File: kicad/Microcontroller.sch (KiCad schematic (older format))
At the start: 30 parts, among them CN4 Conn Vite 1,5x2, CN5 Ventola, CN6 Conn Vite 1,5x2, J7 Reset, J8 Arduino_Nano_Header, U4 MAX6675

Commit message: Schematic update
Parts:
- removed A1, B1, ENC1, OK1: CONN_01X01, symbol CONN_01X01
- removed D2, D3: 1N4148, symbol D
- removed J7: Reset, symbol CONN_01X02
- removed JP1: ~, symbol CONN_01X05
- removed R21, R22, R23: 15K, symbol R
- removed R24: 1K, symbol R
- removed R25: 10K, symbol R
- gave numbers to parts that had none: 2
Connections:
- net labels added: SCK
- net labels removed: CLK, DO, RB3, RB4, RB5, RB6
- wire segments 87 -> 56
- no-connect marks 21 -> 20

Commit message: Modified the Kicad schematic adding the reset to I2c controller
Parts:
- removed R24: R, symbol R
- R25: value R -> 15K
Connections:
- net labels added: Reset
- wire segments 56 -> 53
- no-connect marks 20 -> 17
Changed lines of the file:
@@
-EESchema Schematic File Version 3
+EESchema Schematic File Version 2
 LIBS:HotAirGun-rescue
 LIBS:power
 LIBS:device
+LIBS:transistors
+LIBS:conn
 LIBS:linear
 LIBS:regul
+LIBS:74xx
+LIBS:cmos4000
 LIBS:adc-dac
 LIBS:memory
@@
 LIBS:digital-audio
 LIBS:philips
+LIBS:display
 LIBS:cypress
 LIBS:siliconi
@@
 LIBS:atmel
 LIBS:contrib
-LIBS:w_connectors
+LIBS:valves
 LIBS:max6675
 LIBS:lcd16x2
+LIBS:switches
 LIBS:HotAirGun-cache
-EELAYER 26 0
+EELAYER 25 0
 EELAYER END
 $Descr A4 11693 8268
@@
 L Arduino_Nano_Header J8
 U 1 1 59BC3AFF
-P 5580 4170
-F 0 "J8" H 5580 5107 60  0000 C CNN
-F 1 "Arduino_Nano_Header" H 5580 5001 60  0000 C CNN
-F 2 "" H 5580 4170 60  0000 C CNN
-F 3 "" H 5580 4170 60  0000 C CNN
-	1    5580 4170
-	1    0    0    -1
-$EndComp
-Text GLabel 4535 4270 0    60   Input ~ 0
+P 5670 4230
+F 0 "J8" H 5670 5167 60  0000 C CNN
+F 1 "Arduino_Nano_Header" H 5670 5061 60  0000 C CNN
+F 2 "" H 5670 4230 60  0000 C CNN
+F 3 "" H 5670 4230 60  0000 C CNN
+	1    5670 4230
+	1    0    0    -1
+$EndComp
+Text GLabel 4625 4330 0    60   Input ~ 0
 CS
-Text GLabel 4580 4370 0    60   Input ~ 0
+Text GLabel 4670 4430 0    60   Input ~ 0
 SCK
-Text GLabel 4530 4170 0    60   Input ~ 0
+Text GLabel 4620 4230 0    60   Input ~ 0
 SO
-Text GLabel 6530 4170 2    60   Input ~ 0
+Text GLabel 6620 4230 2    60   Input ~ 0
 SDA
-Text GLabel 6535 4070 2    60   Input ~ 0
+Text GLabel 6625 4130 2    60   Input ~ 0
 SCL
-Text GLabel 4730 3870 0    60   Input ~ 0
+Text GLabel 4820 3930 0    60   Input ~ 0
 FASE_0
-Text GLabel 4580 4770 0    60   Input ~ 0
+Text GLabel 4670 4830 0    60   Input ~ 0
 FAN
-Text GLabel 5090 4470 0    60   Input ~ 0
+Text GLabel 5180 4530 0    60   Input ~ 0
 RELE_SIC_220V
-Text GLabel 4655 4570 0    60   Input ~ 0
+Text GLabel 4745 4630 0    60   Input ~ 0
 TRIAC
 Wire Wire Line
-	6530 4170 5930 4170
-Wire Wire Line
-	4730 3870 5230 3870
-Wire Wire Line
-	4655 4570 5230 4570
-Wire Wire Line
-	5090 4470 5230 4470
+	6620 4230 6020 4230
+Wire Wire Line
+	4820 3930 5320 3930
+Wire Wire Line
+	4745 4630 5320 4630
+Wire Wire Line
+	5180 4530 5320 4530
 $Comp
 L GND #GND_07
@@
 Wire Wire Line
 	4825 6620 4825 6570
-NoConn ~ 5230 3470
-NoConn ~ 5230 3570
-NoConn ~ 5230 3670
-NoConn ~ 5230 3770
-NoConn ~ 5230 4070
-NoConn ~ 5230 4670
-NoConn ~ 5930 4770
-NoConn ~ 5930 4670
-NoConn ~ 5930 4570
-NoConn ~ 5930 4470
-NoConn ~ 5930 4270
-NoConn ~ 5930 3970
-NoConn ~ 5930 3870
-NoConn ~ 5930 3770
-NoConn ~ 5930 3670
-NoConn ~ 5930 3570
-NoConn ~ 5930 3470
-NoConn ~ 5930 4370
-Text GLabel 4785 3970 0    60   Input ~ 0
+NoConn ~ 5320 3530
+NoConn ~ 5320 3630
+NoConn ~ 5320 3730
+NoConn ~ 5320 3830
+NoConn ~ 5320 4130
+NoConn ~ 5320 4730
+NoConn ~ 6020 4830
+NoConn ~ 6020 4730
+NoConn ~ 6020 4630
+NoConn ~ 6020 4530
+NoConn ~ 6020 4330
+NoConn ~ 6020 4030
+NoConn ~ 6020 3930
+NoConn ~ 6020 4430
+Text GLabel 4875 4030 0    60   Input ~ 0
 MCP_INT
 Wire Wire Line
-	4785 3970 5230 3970
-$Comp
-L R R24
-U 1 1 59C972CE
-P 4885 3645
-F 0 "R24" H 4816 3599 50  0000 R CNN
-F 1 "R" H 4816 3690 50  0000 R CNN
-F 2 "" V 4815 3645 50  0001 C CNN
-F 3 "" H 4885 3645 50  0001 C CNN
-	1    4885 3645
-	1    0    0    1
-$EndComp
+	4875 4030 5320 4030
 $Comp
 L R R25
 U 1 1 59C973F4
-P 5035 3645
-F 0 "R25" H 5105 3691 50  0000 L CNN
-F 1 "R" H 5105 3600 50  0000 L CNN
-F 2 "" V 4965 3645 50  0001 C CNN
-F 3 "" H 5035 3645 50  0001 C CNN
-	1    5035 3645
-	1    0    0    -1
-$EndComp
-Wire Wire Line
-	4885 3795 4885 3970
-Connection ~ 4885 3970
-Wire Wire Line
-	5035 3795 5035 3870
-Connection ~ 5035 3870
-$Comp
-L VCC #PWR?
-U 1 1 59C97A40
-P 4955 3385
-F 0 "#PWR?" H 4955 3235 50  0001 C CNN
-F 1 "VCC" H 4955 3535 50  0000 C CNN
-F 2 "" H 4955 3385 50  0000 C CNN
-F 3 "" H 4955 3385 50  0000 C CNN
-	1    4955 3385
-	1    0    0    -1
-$EndComp
-Wire Wire Line
-	4885 3420 5035 3420
-Wire Wire Line
-	4885 3420 4885 3495
-Wire Wire Line
-	5035 3420 5035 3495
-Connection ~ 4955 3420
-Wire Wire Line
-	4955 3385 4955 3425
-Wire Wire Line
-	4580 4370 5230 4370
-Wire Wire Line
-	5230 4270 4535 4270
-Wire Wire Line
-	4530 4170 5230 4170
-Wire Wire Line
-	5230 4770 4580 4770
-Wire Wire Line
-	5930 4070 6535 4070
+P 5030 3658
+F 0 "R25" H 5100 3704 50  0000 L CNN
+F 1 "15K" H 5100 3613 50  0000 L CNN
+F 2 "" V 4960 3658 50  0001 C CNN
+F 3 "" H 5030 3658 50  0001 C CNN
+	1    5030 3658
+	1    0    0    -1
+$EndComp
+Wire Wire Line
+	4670 4430 5320 4430
+Wire Wire Line
+	5320 4330 4625 4330
+Wire Wire Line
+	4620 4230 5320 4230
+Wire Wire Line
+	5320 4830 4670 4830
+Wire Wire Line
+	6020 4130 6625 4130
 $Comp
 L GND #PWR?
@@
 Wire Wire Line
 	10190 1350 10190 1425
-NoConn ~ 5930 4870
-NoConn ~ 5230 4870
+NoConn ~ 6020 4930
+NoConn ~ 5320 4930
+$Comp
+L VCC #PWR?
+U 1 1 59F9064F
+P 5030 3470
+F 0 "#PWR?" H 5030 3320 50  0001 C CNN
+F 1 "VCC" H 5030 3620 50  0000 C CNN
+F 2 "" H 5030 3470 50  0000 C CNN
+F 3 "" H 5030 3470 50  0000 C CNN
+	1    5030 3470
+	1    0    0    -1
+$EndComp
+Wire Wire Line
+	5030 3470 5030 3520
+Wire Wire Line
+	5030 3810 5030 3930
+Connection ~ 5030 3930
+$Comp
+L VCC #PWR?
+U 1 1 59F90C41
+P 6020 3830
+F 0 "#PWR?" H 6020 3680 50  0001 C CNN
+F 1 "VCC" H 6020 3980 50  0000 C CNN
+F 2 "" H 6020 3830 50  0000 C CNN
+F 3 "" H 6020 3830 50  0000 C CNN
+	1    6020 3830
+	0    1    1    0
+$EndComp
+$Comp
+L GND #PWR?
+U 1 1 59F90D0D
+P 6020 3630
+F 0 "#PWR?" H 6020 3380 50  0001 C CNN
+F 1 "GND" H 6020 3480 50  0000 C CNN
+F 2 "" H 6020 3630 50  0000 C CNN
+F 3 "" H 6020 3630 50  0000 C CNN
+	1    6020 3630
+	0    -1   -1   0
+$EndComp
+NoConn ~ 6020 3530
+Text GLabel 6630 3730 2    60   Input ~ 0
+Reset
+Wire Wire Line
+	6020 3730 6630 3730
 $EndSCHEMATC

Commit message: added step-down circuit
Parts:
- removed D4: 1N5819, symbol D
- removed VR1: 7805, symbol 7805
- added D2: 1N5819, symbol D
- added L2: 330uH, symbol L
- added U5: LM2575, symbol LM2575
- C1, C2: value ~ -> CP
- CN4: value Conn Vite 1,5x2 -> ~
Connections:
- net labels added: +24V
- wire segments 53 -> 49
- no-connect marks 17 -> 7
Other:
- moved on the sheet: CN4, CN5, D5, Q2, R25, R26, R27

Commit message: Update the schematic with the safety relays for 220V. Microcontroller page now is connect with the grid.
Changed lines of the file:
@@
 LIBS:lcd16x2
 LIBS:switches
+LIBS:relays
 LIBS:HotAirGun-cache
 EELAYER 25 0
@@
 Text GLabel 3800 2550 0    55   Input ~ 0
 FASE_0
-Text GLabel 3650 3550 0    60   Input ~ 0
+Text GLabel 3650 3450 0    60   Input ~ 0
 FAN
 Text GLabel 3700 3250 0    55   Input ~ 0
 TRIAC
 $Comp
-L GND #GND_8
+L GND #GND_7
 U 1 1 59BCB19E
 P 8650 4800
-F 0 "#GND_8" H 8650 4550 50  0001 C CNN
+F 0 "#GND_7" H 8650 4550 50  0001 C CNN
 F 1 "GND" H 8650 4650 50  0000 C CNN
 F 2 "" H 8650 4800 50  0000 C CNN
@@
 $EndComp
 $Comp
-L GND #GND_10
+L GND #GND_9
 U 1 1 59BCB1A4
 P 9450 4800
-F 0 "#GND_10" H 9450 4550 50  0001 C CNN
+F 0 "#GND_9" H 9450 4550 50  0001 C CNN
 F 1 "GND" H 9450 4650 50  0000 C CNN
 F 2 "" H 9450 4800 50  0000 C CNN
@@
 $EndComp
 $Comp
-L GND #GND_9
+L GND #GND_8
 U 1 1 59BCB4EF
 P 9055 2700
-F 0 "#GND_9" H 9055 2450 50  0001 C CNN
+F 0 "#GND_8" H 9055 2450 50  0001 C CNN
 F 1 "GND" H 9055 2550 50  0000 C CNN
 F 2 "" H 9055 2700 50  0000 C CNN
@@
 $EndComp
 $Comp
-L GND #GND_7
+L GND #GND_6
 U 1 1 59BCB4F5
 P 8605 1660
-F 0 "#GND_7" H 8605 1410 50  0001 C CNN
+F 0 "#GND_6" H 8605 1410 50  0001 C CNN
 F 1 "GND" H 8605 1510 50  0000 C CNN
 F 2 "" H 8605 1660 50  0000 C CNN
@@
 $EndComp
 $Comp
-L GND #PWR28
+L GND #PWR35
 U 1 1 59ECEF91
 P 10190 1425
-F 0 "#PWR28" H 10190 1175 50  0001 C CNN
+F 0 "#PWR35" H 10190 1175 50  0001 C CNN
 F 1 "GND" H 10195 1252 50  0000 C CNN
 F 2 "" H 10190 1425 50  0001 C CNN
@@
 NoConn ~ 5040 3568
 $Comp
-L VCC #PWR25
+L VCC #PWR29
 U 1 1 59F9064F
 P 4050 2099
-F 0 "#PWR25" H 4050 1949 50  0001 C CNN
+F 0 "#PWR29" H 4050 1949 50  0001 C CNN
 F 1 "VCC" H 4050 2249 50  0000 C CNN
 F 2 "" H 4050 2099 50  0000 C CNN
@@
 $EndComp
 $Comp
-L VCC #PWR27
+L VCC #PWR32
 U 1 1 59F90C41
 P 5050 2450
-F 0 "#PWR27" H 5050 2300 50  0001 C CNN
+F 0 "#PWR32" H 5050 2300 50  0001 C CNN
 F 1 "VCC" H 5050 2600 50  0000 C CNN
 F 2 "" H 5050 2450 50  0000 C CNN
@@
 $EndComp
 $Comp
-L GND #PWR26
+L GND #PWR31
 U 1 1 59F90D0D
 P 5050 2250
-F 0 "#PWR26" H 5050 2000 50  0001 C CNN
+F 0 "#PWR31" H 5050 2000 50  0001 C CNN
 F 1 "GND" H 5050 2100 50  0000 C CNN
 F 2 "" H 5050 2250 50  0000 C CNN
@@
 	10190 1350 10190 1425
 Wire Wire Line
-	3650 3550 4350 3550
+	3650 3450 4350 3450
 Wire Wire Line
 	4350 3250 3700 3250
@@
 	2950 5350 3000 5350
 $Comp
-L GND #PWR22
+L GND #PWR25
 U 1 1 59FA9D7C
 P 3000 5350
-F 0 "#PWR22" H 3000 5100 50  0001 C CNN
+F 0 "#PWR25" H 3000 5100 50  0001 C CNN
 F 1 "GND" H 3000 5200 50  0000 C CNN
 F 2 "" H 3000 5350 50  0000 C CNN
@@
 	2950 5450 3550 5450
 $Comp
-L +24V #PWR23
+L +24V #PWR27
 U 1 1 59FAA0E3
 P 3400 5450
-F 0 "#PWR23" H 3400 5300 50  0001 C CNN
+F 0 "#PWR27" H 3400 5300 50  0001 C CNN
 F 1 "+24V" H 3400 5590 50  0000 C CNN
 F 2 "" H 3400 5450 50  0000 C CNN
@@
 	3550 5650 3550 5850
 $Comp
-L GND #PWR24
+L GND #PWR28
 U 1 1 59FAA34A
 P 3550 5750
-F 0 "#PWR24" H 3550 5500 50  0001 C CNN
+F 0 "#PWR28" H 3550 5500 50  0001 C CNN
 F 1 "GND" H 3550 5600 50  0000 C CNN
 F 2 "" H 3550 5750 50  0000 C CNN
@@
 	5300 5750 5600 5750
 $Comp
-L GND #PWR?
+L GND #PWR33
 U 1 1 59FAB3AC
 P 5400 6050
-F 0 "#PWR?" H 5400 5800 50  0001 C CNN
+F 0 "#PWR33" H 5400 5800 50  0001 C CNN
 F 1 "GND" H 5400 5900 50  0000 C CNN
 F 2 "" H 5400 6050 50  0000 C CNN
@@
 $EndComp
 $Comp
-L GND #PWR?
+L GND #PWR30
 U 1 1 59FAB48C
 P 4900 6050
-F 0 "#PWR?" H 4900 5800 50  0001 C CNN
+F 0 "#PWR30" H 4900 5800 50  0001 C CNN
 F 1 "GND" H 4900 5900 50  0000 C CNN
 F 2 "" H 4900 6050 50  0000 C CNN
@@
 $EndComp
 $Comp
-L GND #PWR?
+L GND #PWR26
 U 1 1 59FAB539
 P 3100 5750
-F 0 "#PWR?" H 3100 5500 50  0001 C CNN
+F 0 "#PWR26" H 3100 5500 50  0001 C CNN
 F 1 "GND" H 3100 5600 50  0000 C CNN
 F 2 "" H 3100 5750 50  0000 C CNN
@@
 $EndComp
 $Comp
-L VCC #PWR?
+L VCC #PWR34
 U 1 1 59FAB8E3
 P 5600 5750
-F 0 "#PWR?" H 5600 5600 50  0001 C CNN
+F 0 "#PWR34" H 5600 5600 50  0001 C CNN
 F 1 "VCC" H 5600 5900 50  0000 C CNN
 F 2 "" H 5600 5750 50  0000 C CNN

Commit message: v2
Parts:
- removed CN4: ~, symbol CONN_01X02
- removed CN5: Ventola, symbol CONN_01X02
- removed CN6: Conn Vite 1,5x2, symbol CONN_01X02
- removed D2: 1N5819, symbol D
- removed J8: Arduino_Nano_Header, symbol Arduino_Nano_Header
- removed R25: 15K, symbol R
- removed U5: LM2575, symbol LM2575
- added D6: Led_Ye, LEDs:LED-3MM, symbol LED
- added D7: Led_Bl, LEDs:LED-3MM, symbol LED
- added D8: Led_Gr, LEDs:LED-3MM, symbol LED
- added D9: 1N5819, Diodes_THT:D_DO-35_SOD27_P7.62mm_Horizontal, symbol D
- added J10, J9: CONN_01X06, Pin_Headers:Pin_Header_Straight_1x06, symbol CONN_01X06
- added J7: Vin, Connectors_Phoenix:PhoenixContact_MSTBVA-G_02x5.08mm_Vertical, symbol Screw_Terminal_1x02
- added J8: Foot Switch, Connect:JACK_ALIM, symbol CONN_01X02
- added R15: 2K2, Resistors_SMD:R_0603_HandSoldering, symbol R
- added R16, R17: 470R, Resistors_SMD:R_0603_HandSoldering, symbol R
- added R18: 15K, Resistors_SMD:R_0603_HandSoldering, symbol R
- added U3: LM2575, TO_SOT_Packages_THT:Pentawatt_Neutral_Staggered_Verical_TO220-5-T05D, symbol LM2575
- added XA1: Arduino_Nano_Socket, Arduino:Arduino_Nano_Socket, symbol Arduino_Nano_Socket
- C1, C2: footprint (none) -> Capacitors_THT:CP_Radial_D12.5mm_P7.50mm
- C3: value 10pF -> C; footprint (none) -> Capacitors_SMD:C_0603_HandSoldering
- C4: value ~ -> 100pF; footprint (none) -> Capacitors_SMD:C_0603_HandSoldering
- D10: renamed from D5; value ~ -> BA159; footprint (none) -> Diodes_THT:D_DO-41_SOD81_P10.16mm_Horizontal
- L2: footprint (none) -> Choke_Radial_ThroughHole:Choke_Radial_27mm_2,8mm-Drills_CD_Bobin_Type_No1410311
- Q3: renamed from Q2; value ~ -> IRF740; footprint (none) -> TO_SOT_Packages_THT:TO-220_Vertical
- R19: renamed from R26; value R21 -> 10K; footprint (none) -> Resistors_SMD:R_0603_HandSoldering
- R20: renamed from R27; footprint (none) -> Resistors_SMD:R_0603_HandSoldering
- U4: footprint (none) -> Housings_SOIC:SOIC-8_3.9x4.9mm_Pitch1.27mm
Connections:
- net labels added: 0_FASE, D_LED, Earth, FOOT_SW, SAFE_REL, TILT
- net labels removed: +12V, FASE_0, RELE_SIC_220V, Reset, TC+, TC-
- wire segments 49 -> 46
- no-connect marks 7 -> 14
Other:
- note added: "3 Tilt switch"
- note added: "Gun Connector defintion \n"
- note removed: "3 Standby switch"
- moved on the sheet: D10, Q3, R19, R20

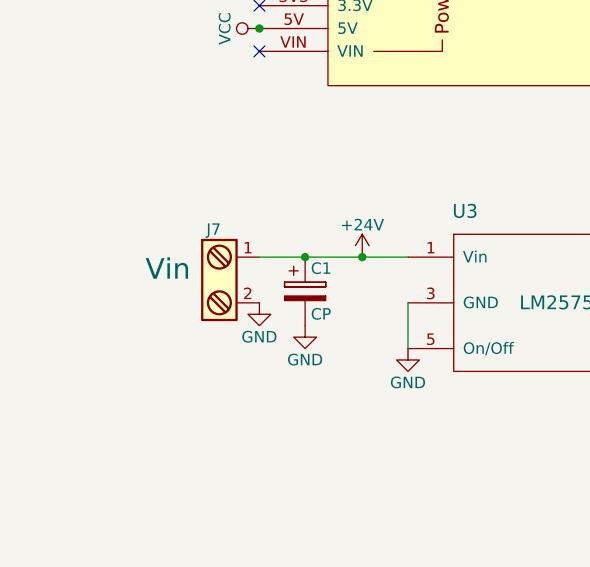
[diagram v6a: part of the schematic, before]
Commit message: New PCB version with smd component Added plot folder with gerber file
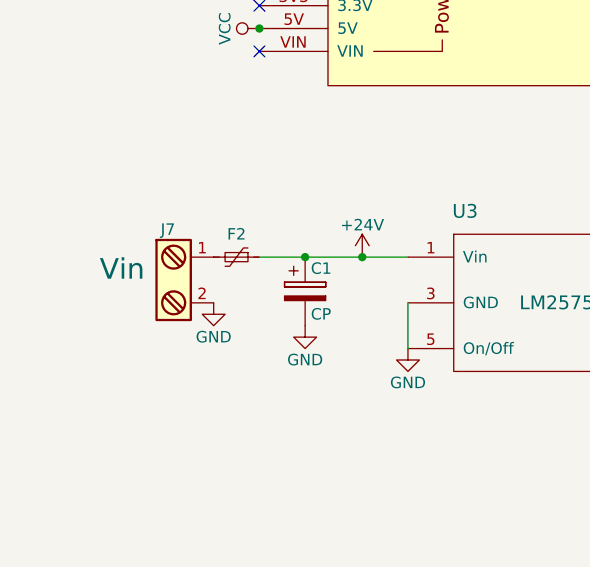
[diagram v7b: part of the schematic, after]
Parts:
- added F2: Polyfuse_Small, Fuse_Holders_and_Fuses:Fuse_TE5_Littlefuse-395Series, symbol Polyfuse_Small
- J8: footprint Connect:JACK_ALIM -> Connectors_Molex:Molex_KK-6410-02_02x2.54mm_Straight
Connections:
- net +24V: now also F2.1; no longer J7.1
- new net: F2.2, J7.1
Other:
- moved on the sheet: J7
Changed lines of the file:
@@
 F 0 "J8" H 4300 6550 50  0000 C CNN
 F 1 "Foot Switch" V 4400 6400 50  0000 C CNN
-F 2 "Connect:JACK_ALIM" H 4300 6400 50  0001 C CNN
+F 2 "Connectors_Molex:Molex_KK-6410-02_02x2.54mm_Straight" H 4300 6400 50  0001 C CNN
 F 3 "" H 4300 6400 50  0001 C CNN
 	1    4300 6400
@@
 L Screw_Terminal_1x02 J7
 U 1 1 5C07171E
-P 1950 4600
-F 0 "J7" H 1950 4850 50  0000 C TNN
-F 1 "Vin" H 1750 4700 90  0000 C TNN
-F 2 "Connectors_Phoenix:PhoenixContact_MSTBVA-G_02x5.08mm_Vertical" H 1950 4375 50  0001 C CNN
-F 3 "" H 1925 4600 50  0001 C CNN
-	1    1950 4600
+P 1750 4600
+F 0 "J7" H 1750 4850 50  0000 C TNN
+F 1 "Vin" H 1550 4700 90  0000 C TNN
+F 2 "Connectors_Phoenix:PhoenixContact_MSTBVA-G_02x5.08mm_Vertical" H 1750 4375 50  0001 C CNN
+F 3 "" H 1725 4600 50  0001 C CNN
+	1    1750 4600
 	1    0    0    -1
 $EndComp
@@
 L GND #PWR028
 U 1 1 5C071989
-P 2150 4700
-F 0 "#PWR028" H 2150 4450 50  0001 C CNN
-F 1 "GND" H 2150 4550 50  0000 C CNN
-F 2 "" H 2150 4700 50  0000 C CNN
-F 3 "" H 2150 4700 50  0000 C CNN
-	1    2150 4700
+P 1950 4700
+F 0 "#PWR028" H 1950 4450 50  0001 C CNN
+F 1 "GND" H 1950 4550 50  0000 C CNN
+F 2 "" H 1950 4700 50  0000 C CNN
+F 3 "" H 1950 4700 50  0000 C CNN
+	1    1950 4700
 	1    0    0    -1
 $EndComp
@@
 Wire Wire Line
 	7950 2650 7450 2650
+$Comp
+L Polyfuse_Small F2
+U 1 1 5C22A5BD
+P 2050 4500
+F 0 "F2" V 1950 4500 50  0000 C CNN
+F 1 "Polyfuse_Small" V 2125 4500 50  0001 C CNN
+F 2 "Fuse_Holders_and_Fuses:Fuse_TE5_Littlefuse-395Series" H 2100 4300 50  0001 L CNN
+F 3 "" H 2050 4500 50  0001 C CNN
+	1    2050 4500
+	0    1    1    0
+$EndComp
 $EndSCHEMATC

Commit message: Update with new PCB version
Kicad schematic and pcb layout correction on Mosfet and Triac footprint.
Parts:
- C1: value CP -> 100uF
- C2: value CP -> 470uF
- D10: footprint Diodes_THT:D_DO-41_SOD81_P10.16mm_Horizontal -> Discret:D4
- F2: footprint Fuse_Holders_and_Fuses:Fuse_TE5_Littlefuse-395Series -> Fuse_Holders_and_Fuses:Fuseholder5x20_horiz_open_Schurter_0031_8201
- J8: footprint Connectors_Molex:Molex_KK-6410-02_02x2.54mm_Straight -> Connect:JACK_ALIM
- L2: footprint Choke_Radial_ThroughHole:Choke_Radial_27mm_2,8mm-Drills_CD_Bobin_Type_No1410311 -> Msystem:Induttanza
- Q3: symbol Q_NMOS_DGS -> Q_PMOS_GDS
- R18: value 15K -> 12K
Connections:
- net Earth: now also C3.1, J10.1 (P1), U4.2 (TC-)
- net at D10.1 (K), J10.6 (P6): now also Q3.2 (D); no longer Q3.1 (D)
- net at R20.1: now also Q3.1 (G); no longer Q3.2 (G)
- net TILT renamed S_SW
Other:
- note added: "3 Stand switch"
- note removed: "3 Tilt switch"
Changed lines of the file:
@@
 2 - K Thermocouple
 Text Notes 10049 5843 0    60   ~ 0
-3 Tilt switch
+3 Stand switch
 Text Notes 10049 5943 0    60   ~ 0
 4 Groung Steel Tube
@@
 $EndComp
 $Comp
-L Q_NMOS_DGS Q3
+L Q_PMOS_GDS Q3
 U 1 1 59BCB1B0
 P 9400 3700
@@
 F 0 "D10" H 9900 3750 50  0000 C CNN
 F 1 "BA159" H 9900 3550 50  0000 C CNN
-F 2 "Diodes_THT:D_DO-41_SOD81_P10.16mm_Horizontal" H 9900 3650 50  0001 C CNN
+F 2 "Discret:D4" H 9900 3650 50  0001 C CNN
 F 3 "" H 9900 3650 50  0000 C CNN
 	1    9900 3650
@@
 P 4750 1500
 F 0 "R18" V 4830 1500 50  0000 C CNN
-F 1 "15K" V 4750 1500 50  0000 C CNN
+F 1 "12K" V 4750 1500 50  0000 C CNN
 F 2 "Resistors_SMD:R_0603_HandSoldering" V 4680 1500 50  0001 C CNN
 F 3 "" H 4750 1500 50  0001 C CNN
@@
 $EndComp
 Text GLabel 8150 2700 3    60   Input ~ 0
-TILT
+S_SW
 $Comp
 L Earth #PWR023
@@
 F 0 "J8" H 4300 6550 50  0000 C CNN
 F 1 "Foot Switch" V 4400 6400 50  0000 C CNN
-F 2 "Connectors_Molex:Molex_KK-6410-02_02x2.54mm_Straight" H 4300 6400 50  0001 C CNN
+F 2 "Connect:JACK_ALIM" H 4300 6400 50  0001 C CNN
 F 3 "" H 4300 6400 50  0001 C CNN
 	1    4300 6400
@@
 F 0 "L2" V 4300 4800 50  0000 C CNN
 F 1 "330uH" V 4425 4800 50  0000 C CNN
-F 2 "Choke_Radial_ThroughHole:Choke_Radial_27mm_2,8mm-Drills_CD_Bobin_Type_No1410311" H 4350 4800 50  0001 C CNN
+F 2 "Msystem:Induttanza" H 4350 4800 50  0001 C CNN
 F 3 "" H 4350 4800 50  0000 C CNN
 	1    4350 4800
@@
 P 4600 4950
 F 0 "C2" H 4625 5050 50  0000 L CNN
-F 1 "CP" H 4625 4850 50  0000 L CNN
+F 1 "470uF" H 4625 4850 50  0000 L CNN
 F 2 "Capacitors_THT:CP_Radial_D12.5mm_P7.50mm" H 4638 4800 50  0001 C CNN
 F 3 "" H 4600 4950 50  0000 C CNN
@@
 P 2350 4650
 F 0 "C1" H 2375 4750 50  0000 L CNN
-F 1 "CP" H 2375 4550 50  0000 L CNN
+F 1 "100uF" H 2375 4550 50  0000 L CNN
 F 2 "Capacitors_THT:CP_Radial_D12.5mm_P7.50mm" H 2388 4500 50  0001 C CNN
 F 3 "" H 2350 4650 50  0000 C CNN
@@
 Text GLabel 5150 2900 2    60   Input ~ 0
 D_LED
-Text GLabel 1700 2700 0    60   Input ~ 0
+Text GLabel 1650 2700 0    60   Input ~ 0
 FOOT_SW
 Text GLabel 1950 2600 0    60   Input ~ 0
-TILT
+S_SW
 Text GLabel 5200 3700 0    60   Input ~ 0
 SCL
@@
 Text GLabel 1950 2400 0    60   Input ~ 0
 SCL
-Text GLabel 1700 2500 0    60   Input ~ 0
+Text GLabel 1650 2500 0    60   Input ~ 0
 SDA
 Text GLabel 5400 1900 2    55   Input ~ 0
@@
 	5150 2900 4750 2900
 Wire Wire Line
-	1700 2700 2150 2700
+	1650 2700 2150 2700
 Wire Wire Line
 	1950 2600 2150 2600
@@
 	1950 2400 2150 2400
 Wire Wire Line
-	1700 2500 2150 2500
+	1650 2500 2150 2500
 Wire Wire Line
 	5400 1900 4750 1900
@@
 F 0 "F2" V 1950 4500 50  0000 C CNN
 F 1 "Polyfuse_Small" V 2125 4500 50  0001 C CNN
-F 2 "Fuse_Holders_and_Fuses:Fuse_TE5_Littlefuse-395Series" H 2100 4300 50  0001 L CNN
+F 2 "Fuse_Holders_and_Fuses:Fuseholder5x20_horiz_open_Schurter_0031_8201" H 2100 4300 50  0001 L CNN
 F 3 "" H 2050 4500 50  0001 C CNN
 	1    2050 4500
 	0    1    1    0
 $EndComp
+$Comp
+L Earth #PWR031
+U 1 1 5C3C5FBA
+P 7450 3050
+F 0 "#PWR031" H 7450 2800 50  0001 C CNN
+F 1 "Earth" H 7450 2900 50  0001 C CNN
+F 2 "" H 7450 3050 50  0001 C CNN
+F 3 "" H 7450 3050 50  0001 C CNN
+	1    7450 3050
+	0    -1   -1   0
+$EndComp
 $EndSCHEMATC
